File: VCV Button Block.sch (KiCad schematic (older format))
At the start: 20 parts, among them SW41 B3F-5050, SW42 B3F-5050, SW43 B3F-5050, SW44 B3F-5050, SW45 B3F-5050, SW46 B3F-5050, SW47 B3F-5050, SW48 B3F-5050, SW49 B3F-5050, SW50 B3F-5050, SW51 B3F-5050, SW52 B3F-5050, SW53 B3F-5050, SW54 B3F-5050, SW55 B3F-5050, SW56 B3F-5050, U4 CD74HC4067M

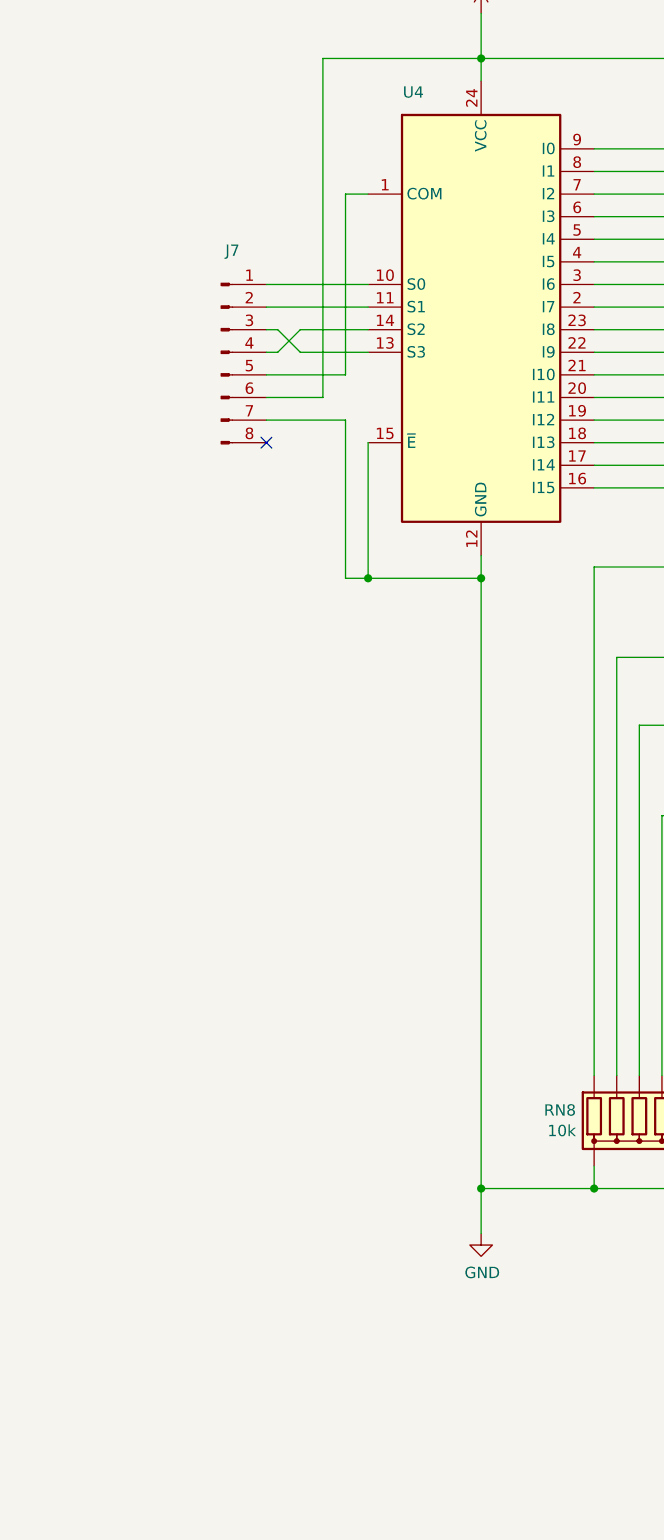
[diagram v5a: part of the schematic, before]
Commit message: Further cleanup and placement
Removed all the connectors to the rails as they're irrelevant to the top boards.

Added all the support headers.

Need to work out the correct routing for the headers but the placement is correct.
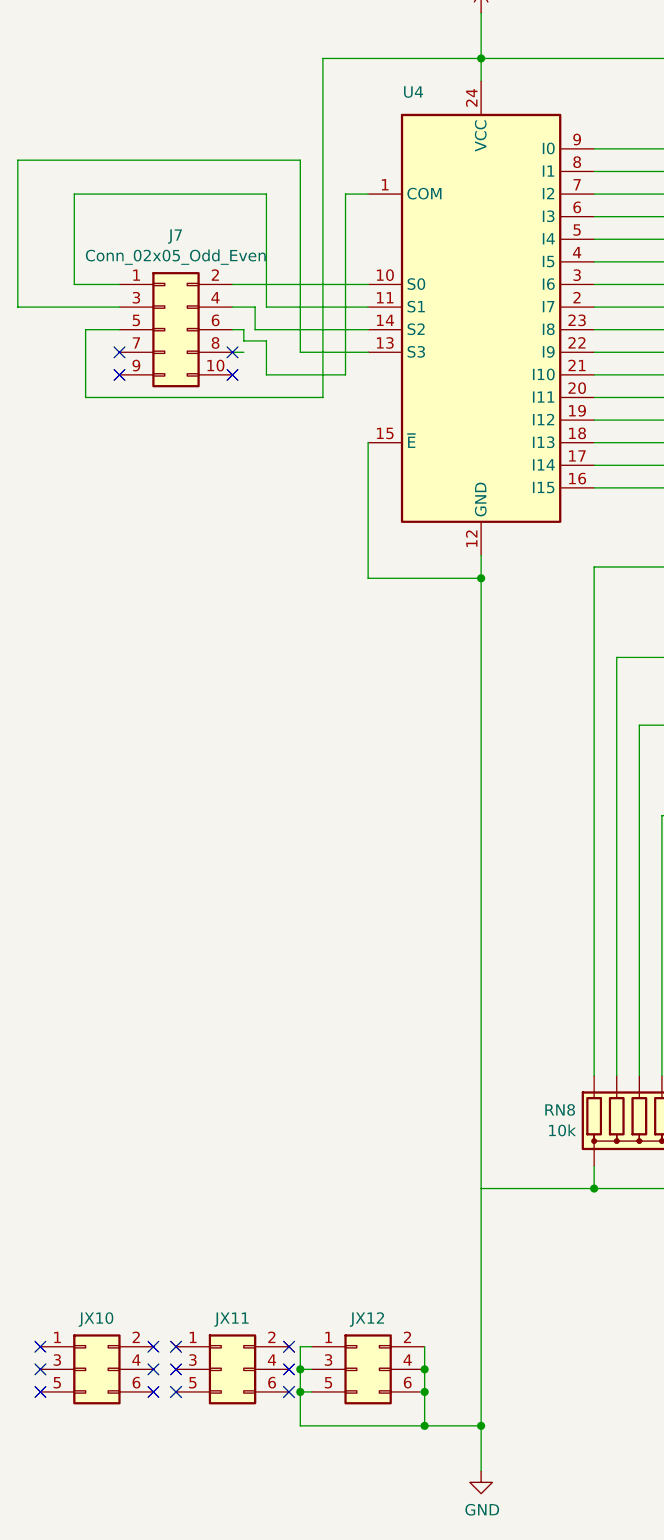
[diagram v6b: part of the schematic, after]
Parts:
- removed J7: ~, cunabulapress-footprints:Connector_TE_Connectivity_Micro-MaTch_8_Position_Female, symbol Connector:Conn_01x08_Male
- added J7: Conn_02x05_Odd_Even, Connector_PinHeader_2.54mm:PinHeader_2x05_P2.54mm_Vertical, symbol Connector_Generic:Conn_02x05_Odd_Even
- added JX10, JX11, JX12: Conn_02x03_Odd_Even, Connector_PinHeader_2.54mm:PinHeader_2x03_P2.54mm_Vertical, symbol Connector_Generic:Conn_02x03_Odd_Even
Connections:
- net +5V: now also J7.5 (Pin_5)
- net GND: now also JX12.1 (Pin_1), JX12.2 (Pin_2), JX12.3 (Pin_3), JX12.4 (Pin_4), JX12.5 (Pin_5), JX12.6 (Pin_6); no longer RN8.1 (common), RN9.1 (common)
- net at U4.1 (COM): now also J7.6 (Pin_6)
- net at U4.10 (S0): now also J7.2 (Pin_2)
- net at U4.11 (S1): now also J7.1 (Pin_1)
- net at U4.13 (S3): now also J7.3 (Pin_3)
- net at U4.14 (S2): now also J7.4 (Pin_4)
- new net: RN8.1 (common), RN9.1 (common)
- no-connect marks 33 -> 48
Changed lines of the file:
@@
 $Descr A4 11693 8268
 encoding utf-8
-Sheet 9 9
+Sheet 8 8
 Title ""
 Date ""
-Rev ""
+Rev "v3"
 Comp ""
 Comment1 ""
@@
 	1    0    0    -1
 $EndComp
-$Comp
-L power:GND #PWR?
-U 1 1 5C60FBB6
-P 2700 6350
-AR Path="/5C4B73B3/5C60FBB6" Ref="#PWR?"  Part="1"
-AR Path="/5C4BAA18/5C60FBB6" Ref="#PWR022"  Part="1"
-F 0 "#PWR022" H 2700 6100 50  0001 C CNN
-F 1 "GND" H 2705 6177 50  0000 C CNN
-F 2 "" H 2700 6350 50  0001 C CNN
-F 3 "" H 2700 6350 50  0001 C CNN
-	1    2700 6350
-	1    0    0    -1
-$EndComp
 Wire Wire Line
 	2200 2850 2200 3450
@@
 	2700 950  2700 1150
 NoConn ~ 7700 2500
-$Comp
-L Connector:Conn_01x08_Male J?
-U 1 1 5CE6340D
-P 1550 2450
-AR Path="/5C3B66BD/5CE6340D" Ref="J?"  Part="1"
-AR Path="/5C4BAA18/5CE6340D" Ref="J7"  Part="1"
-F 0 "J7" H 1600 2900 50  0000 C CNN
-F 1 "~" H 1444 2844 50  0000 C CNN
-F 2 "cunabulapress-footprints:Connector_TE_Connectivity_Micro-MaTch_8_Position_Female" H 1550 2450 50  0001 C CNN
-F 3 "~" H 1550 2450 50  0001 C CNN
-	1    1550 2450
-	1    0    0    -1
-$EndComp
-NoConn ~ 1750 2850
 Wire Wire Line
 	2000 2650 2000 1150
@@
 Wire Wire Line
 	2700 1150 2700 1250
-Wire Wire Line
-	1750 2350 1800 2350
-Wire Wire Line
-	1800 2350 1900 2450
-Wire Wire Line
-	1900 2350 1800 2450
-Wire Wire Line
-	1800 2450 1750 2450
 Connection ~ 2700 3450
 NoConn ~ 7300 2500
@@
 $EndComp
 Wire Wire Line
-	1750 2650 2000 2650
-Wire Wire Line
-	2700 3450 2700 6150
-Wire Wire Line
 	3200 3050 4000 3050
 Wire Wire Line
@@
 	3200 6150 2700 6150
 Wire Wire Line
-	2700 6150 2700 6350
-Connection ~ 2700 6150
-Wire Wire Line
 	7100 2600 7300 2600
 Wire Wire Line
@@
 	7700 5400 7900 5400
 Wire Wire Line
-	2200 3450 2100 3450
-Wire Wire Line
-	2100 3450 2100 2750
-Connection ~ 2200 3450
+	2100 2550 2100 1750
+Wire Wire Line
+	2100 1750 2200 1750
+Wire Wire Line
+	2000 1150 2700 1150
 Wire Wire Line
 	1750 2550 2100 2550
 Wire Wire Line
-	2100 2550 2100 1750
-Wire Wire Line
-	2100 1750 2200 1750
-Wire Wire Line
 	1900 2450 2200 2450
 Wire Wire Line
-	1900 2350 2200 2350
-Wire Wire Line
 	1750 2250 2200 2250
-Wire Wire Line
-	1750 2150 2200 2150
-Wire Wire Line
-	1750 2750 2100 2750
-Wire Wire Line
-	2000 1150 2700 1150
+$Comp
+L Connector_Generic:Conn_02x05_Odd_Even J?
+U 1 1 5D6E6331
+P 1300 2350
+AR Path="/5C4B73B3/5D6E6331" Ref="J?"  Part="1"
+AR Path="/5C4BAA18/5D6E6331" Ref="J7"  Part="1"
+F 0 "J7" H 1350 2767 50  0000 C CNN
+F 1 "Conn_02x05_Odd_Even" H 1350 2676 50  0000 C CNN
+F 2 "Connector_PinHeader_2.54mm:PinHeader_2x05_P2.54mm_Vertical" H 1300 2350 50  0001 C CNN
+F 3 "~" H 1300 2350 50  0001 C CNN
+	1    1300 2350
+	1    0    0    -1
+$EndComp
+Wire Wire Line
+	1600 2150 2200 2150
+Wire Wire Line
+	1750 2250 1750 1750
+Wire Wire Line
+	1750 1750 900  1750
+Wire Wire Line
+	900  1750 900  2150
+Wire Wire Line
+	900  2150 1100 2150
+Wire Wire Line
+	1700 2350 1700 2250
+Wire Wire Line
+	1700 2250 1600 2250
+Wire Wire Line
+	1700 2350 2200 2350
+Wire Wire Line
+	1900 2450 1900 1600
+Wire Wire Line
+	1900 1600 650  1600
+Wire Wire Line
+	650  2250 1100 2250
+Wire Wire Line
+	1750 2550 1750 2400
+Wire Wire Line
+	1750 2400 1650 2400
+Wire Wire Line
+	1650 2400 1650 2350
+Wire Wire Line
+	1650 2350 1600 2350
+Wire Wire Line
+	950  2650 950  2350
+Wire Wire Line
+	950  2350 1100 2350
+Wire Wire Line
+	950  2650 2000 2650
+Wire Wire Line
+	1650 2450 1600 2450
+NoConn ~ 1100 2450
+NoConn ~ 1100 2550
+NoConn ~ 1600 2550
+NoConn ~ 1600 2450
+Wire Wire Line
+	650  1600 650  2250
+$Comp
+L power:GND #PWR?
+U 1 1 5D912B99
+P 2700 7400
+AR Path="/5C4B73B3/5D912B99" Ref="#PWR?"  Part="1"
+AR Path="/5C4BAA18/5D912B99" Ref="#PWR0103"  Part="1"
+F 0 "#PWR0103" H 2700 7150 50  0001 C CNN
+F 1 "GND" H 2705 7227 50  0000 C CNN
+F 2 "" H 2700 7400 50  0001 C CNN
+F 3 "" H 2700 7400 50  0001 C CNN
+	1    2700 7400
+	1    0    0    -1
+$EndComp
+$Comp
+L Connector_Generic:Conn_02x03_Odd_Even JX?
+U 1 1 5D912B9F
+P 950 6950
+AR Path="/5C4B73B3/5D912B9F" Ref="JX?"  Part="1"
+AR Path="/5C4BAA18/5D912B9F" Ref="JX10"  Part="1"
+F 0 "JX10" H 1000 7175 50  0000 C CNN
+F 1 "Conn_02x03_Odd_Even" H 1000 7176 50  0001 C CNN
+F 2 "Connector_PinHeader_2.54mm:PinHeader_2x03_P2.54mm_Vertical" H 950 6950 50  0001 C CNN
+F 3 "~" H 950 6950 50  0001 C CNN
+	1    950  6950
+	1    0    0    -1
+$EndComp
+$Comp
+L Connector_Generic:Conn_02x03_Odd_Even JX?
+U 1 1 5D912BA6
+P 2150 6950
+AR Path="/5C4B73B3/5D912BA6" Ref="JX?"  Part="1"
+AR Path="/5C4BAA18/5D912BA6" Ref="JX12"  Part="1"
+F 0 "JX12" H 2200 7175 50  0000 C CNN
+F 1 "Conn_02x03_Odd_Even" H 2200 7176 50  0001 C CNN
+F 2 "Connector_PinHeader_2.54mm:PinHeader_2x03_P2.54mm_Vertical" H 2150 6950 50  0001 C CNN
+F 3 "~" H 2150 6950 50  0001 C CNN
+	1    2150 6950
+	1    0    0    -1
+$EndComp
+Wire Wire Line
+	2700 7200 2700 7400
+Connection ~ 2700 7200
+Wire Wire Line
+	2450 6850 2450 6950
+Wire Wire Line
+	2450 7200 2700 7200
+Connection ~ 2450 6950
+Wire Wire Line
+	2450 6950 2450 7050
+Connection ~ 2450 7050
+Wire Wire Line
+	2450 7050 2450 7200
+$Comp
+L Connector_Generic:Conn_02x03_Odd_Even JX?
+U 1 1 5D912BB6
+P 1550 6950
+AR Path="/5C4B73B3/5D912BB6" Ref="JX?"  Part="1"
+AR Path="/5C4BAA18/5D912BB6" Ref="JX11"  Part="1"
+F 0 "JX11" H 1600 7175 50  0000 C CNN
+F 1 "Conn_02x03_Odd_Even" H 1600 7176 50  0001 C CNN
+F 2 "Connector_PinHeader_2.54mm:PinHeader_2x03_P2.54mm_Vertical" H 1550 6950 50  0001 C CNN
+F 3 "~" H 1550 6950 50  0001 C CNN
+	1    1550 6950
+	1    0    0    -1
+$EndComp
+Wire Wire Line
+	1900 6850 1900 6950
+Wire Wire Line
+	1900 7200 2450 7200
+Connection ~ 2450 7200
+Wire Wire Line
+	1950 7050 1900 7050
+Connection ~ 1900 7050
+Wire Wire Line
+	1900 7050 1900 7200
+Wire Wire Line
+	1950 6950 1900 6950
+Connection ~ 1900 6950
+Wire Wire Line
+	1900 6950 1900 7050
+Wire Wire Line
+	1950 6850 1900 6850
+NoConn ~ 1850 6850
+NoConn ~ 1850 6950
+NoConn ~ 1850 7050
+NoConn ~ 1350 7050
+NoConn ~ 1350 6950
+NoConn ~ 1350 6850
+NoConn ~ 1250 6850
+NoConn ~ 1250 6950
+NoConn ~ 1250 7050
+NoConn ~ 750  6850
+NoConn ~ 750  6950
+NoConn ~ 750  7050
+Wire Wire Line
+	2700 3450 2700 7200
 $EndSCHEMATC

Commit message: All subsidiary boards complete
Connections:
- net GND: now also RN8.1 (common), RN9.1 (common)
- net at U4.10 (S0): now also J7.1 (Pin_1); no longer J7.2 (Pin_2)
- net at U4.11 (S1): now also J7.2 (Pin_2); no longer J7.1 (Pin_1)
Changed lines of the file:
@@
 	3200 6050 3200 6150
-Wire Wire Line
-	3200 6150 2700 6150
 Wire Wire Line
 	7100 2600 7300 2600
@@
 Wire Wire Line
 	5600 6150 3200 6150
-Connection ~ 3200 6150
 Wire Wire Line
 	6400 2250 3200 2250
@@
 Wire Wire Line
 	1900 2450 2200 2450
-Wire Wire Line
-	1750 2250 2200 2250
 $Comp
 L Connector_Generic:Conn_02x05_Odd_Even J?
@@
 AR Path="/5C4BAA18/5D6E6331" Ref="J7"  Part="1"
 F 0 "J7" H 1350 2767 50  0000 C CNN
-F 1 "Conn_02x05_Odd_Even" H 1350 2676 50  0000 C CNN
+F 1 "Conn_02x05_Odd_Even" H 1350 2676 50  0001 C CNN
 F 2 "Connector_PinHeader_2.54mm:PinHeader_2x05_P2.54mm_Vertical" H 1300 2350 50  0001 C CNN
 F 3 "~" H 1300 2350 50  0001 C CNN
@@
 $EndComp
 Wire Wire Line
-	1600 2150 2200 2150
-Wire Wire Line
-	1750 2250 1750 1750
-Wire Wire Line
-	1750 1750 900  1750
-Wire Wire Line
-	900  1750 900  2150
-Wire Wire Line
-	900  2150 1100 2150
-Wire Wire Line
-	1700 2350 1700 2250
-Wire Wire Line
-	1700 2250 1600 2250
-Wire Wire Line
-	1700 2350 2200 2350
-Wire Wire Line
-	1900 2450 1900 1600
-Wire Wire Line
-	1900 1600 650  1600
-Wire Wire Line
-	650  2250 1100 2250
-Wire Wire Line
 	1750 2550 1750 2400
 Wire Wire Line
@@
 Wire Wire Line
 	950  2650 2000 2650
-Wire Wire Line
-	1650 2450 1600 2450
 NoConn ~ 1100 2450
 NoConn ~ 1100 2550
 NoConn ~ 1600 2550
 NoConn ~ 1600 2450
-Wire Wire Line
-	650  1600 650  2250
 $Comp
 L power:GND #PWR?
@@
 NoConn ~ 750  7050
 Wire Wire Line
-	2700 3450 2700 7200
+	2700 3450 2700 6150
+Wire Wire Line
+	2200 2150 2200 1900
+Wire Wire Line
+	2200 1900 900  1900
+Wire Wire Line
+	900  1900 900  2150
+Wire Wire Line
+	900  2150 1100 2150
+Wire Wire Line
+	1600 2150 2150 2150
+Wire Wire Line
+	2150 2150 2150 2250
+Wire Wire Line
+	2150 2250 2200 2250
+Wire Wire Line
+	2200 2350 1950 2350
+Wire Wire Line
+	1950 2350 1950 2250
+Wire Wire Line
+	1950 2250 1600 2250
+Wire Wire Line
+	1100 2250 1000 2250
+Wire Wire Line
+	1000 2250 1000 2000
+Wire Wire Line
+	1000 2000 1900 2000
+Wire Wire Line
+	1900 2000 1900 2450
+Wire Wire Line
+	3200 6150 2700 6150
+Connection ~ 3200 6150
+Connection ~ 2700 6150
+Wire Wire Line
+	2700 6150 2700 7200
 $EndSCHEMATC

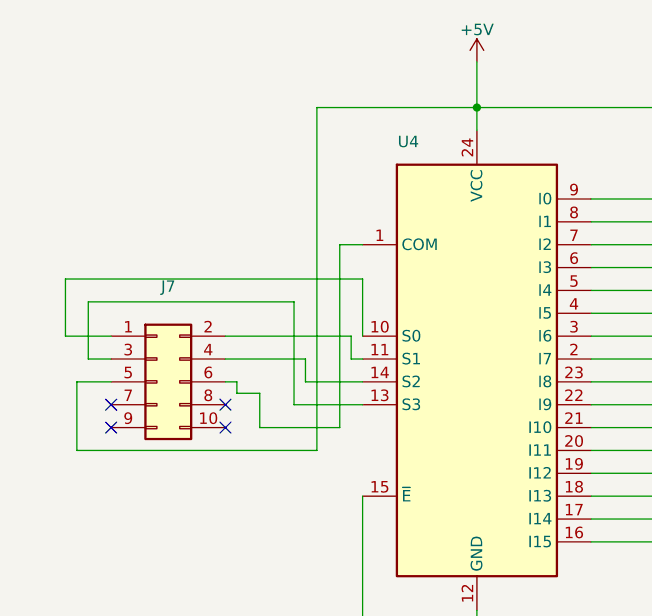
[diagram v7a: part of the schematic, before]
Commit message: Housekeeping
Cleaned up the schematic for the subsidiary boards

Switched 5v and Com connections to make routing easier.
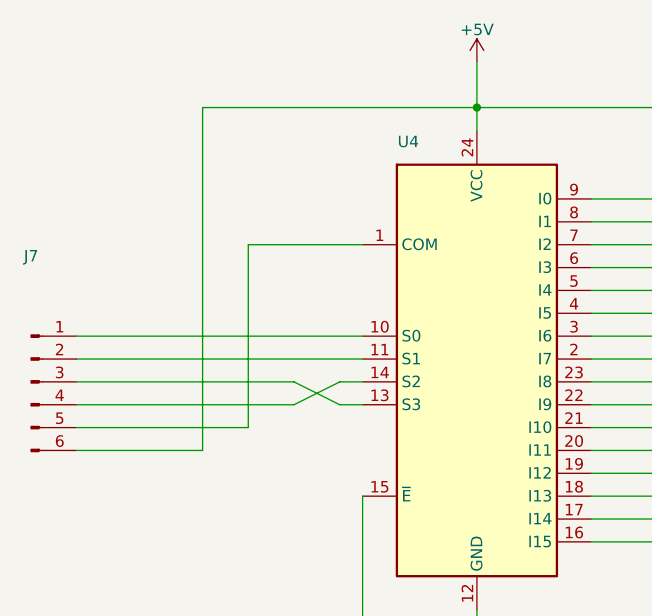
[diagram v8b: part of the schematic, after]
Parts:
- removed J7: Conn_02x05_Odd_Even, Connector_PinHeader_2.54mm:PinHeader_2x05_P2.54mm_Vertical, symbol Connector_Generic:Conn_02x05_Odd_Even
- added J7: Conn_02x05_Odd_Even, Connector_PinHeader_2.54mm:PinHeader_2x03_P2.54mm_Vertical, symbol Connector:Conn_01x06_Male
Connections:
- net +5V: now also J7.6 (Pin_6)
- net at U4.1 (COM): now also J7.5 (Pin_5)
- net at U4.10 (S0): now also J7.1 (Pin_1)
- net at U4.11 (S1): now also J7.2 (Pin_2)
- net at U4.13 (S3): now also J7.3 (Pin_3)
- net at U4.14 (S2): now also J7.4 (Pin_4)
- no-connect marks 48 -> 44
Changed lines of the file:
@@
-	1    0    0    -1
-$EndComp
-$Comp
-L 74xx:CD74HC4067M U?
-U 1 1 5C60FB42
-P 2700 2250
-AR Path="/5C4B73B3/5C60FB42" Ref="U?"  Part="1"
-AR Path="/5C4BAA18/5C60FB42" Ref="U4"  Part="1"
-F 0 "U4" H 2400 3200 50  0000 C CNN
-F 1 "CD74HC4067M" H 2700 3337 50  0001 C CNN
-F 2 "Package_SO:SOIC-24W_7.5x15.4mm_P1.27mm" H 3600 1250 50  0001 C CIN
-F 3 "http://www.ti.com/lit/ds/symlink/cd74hc4067.pdf" H 2350 3100 50  0001 C CNN
-	1    2700 2250
 	1    0    0    -1
 $EndComp
@@
 	2700 950  2700 1150
 NoConn ~ 7700 2500
-Wire Wire Line
-	2000 2650 2000 1150
 Connection ~ 2700 1150
 Wire Wire Line
@@
 Wire Wire Line
 	7700 5400 7900 5400
-Wire Wire Line
-	2100 2550 2100 1750
-Wire Wire Line
-	2100 1750 2200 1750
-Wire Wire Line
-	2000 1150 2700 1150
-Wire Wire Line
-	1750 2550 2100 2550
-Wire Wire Line
-	1900 2450 2200 2450
-$Comp
-L Connector_Generic:Conn_02x05_Odd_Even J?
-U 1 1 5D6E6331
-P 1300 2350
-AR Path="/5C4B73B3/5D6E6331" Ref="J?"  Part="1"
-AR Path="/5C4BAA18/5D6E6331" Ref="J7"  Part="1"
-F 0 "J7" H 1350 2767 50  0000 C CNN
-F 1 "Conn_02x05_Odd_Even" H 1350 2676 50  0001 C CNN
-F 2 "Connector_PinHeader_2.54mm:PinHeader_2x05_P2.54mm_Vertical" H 1300 2350 50  0001 C CNN
-F 3 "~" H 1300 2350 50  0001 C CNN
-	1    1300 2350
-	1    0    0    -1
-$EndComp
-Wire Wire Line
-	1750 2550 1750 2400
-Wire Wire Line
-	1750 2400 1650 2400
-Wire Wire Line
-	1650 2400 1650 2350
-Wire Wire Line
-	1650 2350 1600 2350
-Wire Wire Line
-	950  2650 950  2350
-Wire Wire Line
-	950  2350 1100 2350
-Wire Wire Line
-	950  2650 2000 2650
-NoConn ~ 1100 2450
-NoConn ~ 1100 2550
-NoConn ~ 1600 2550
-NoConn ~ 1600 2450
 $Comp
 L power:GND #PWR?
@@
 	2700 3450 2700 6150
 Wire Wire Line
-	2200 2150 2200 1900
-Wire Wire Line
-	2200 1900 900  1900
-Wire Wire Line
-	900  1900 900  2150
-Wire Wire Line
-	900  2150 1100 2150
-Wire Wire Line
-	1600 2150 2150 2150
-Wire Wire Line
-	2150 2150 2150 2250
-Wire Wire Line
-	2150 2250 2200 2250
-Wire Wire Line
-	2200 2350 1950 2350
-Wire Wire Line
-	1950 2350 1950 2250
-Wire Wire Line
-	1950 2250 1600 2250
-Wire Wire Line
-	1100 2250 1000 2250
-Wire Wire Line
-	1000 2250 1000 2000
-Wire Wire Line
-	1000 2000 1900 2000
-Wire Wire Line
-	1900 2000 1900 2450
-Wire Wire Line
 	3200 6150 2700 6150
 Connection ~ 3200 6150
@@
 Wire Wire Line
 	2700 6150 2700 7200
+$Comp
+L 74xx:CD74HC4067M U?
+U 1 1 5C60FB42
+P 2700 2250
+AR Path="/5C4B73B3/5C60FB42" Ref="U?"  Part="1"
+AR Path="/5C4BAA18/5C60FB42" Ref="U4"  Part="1"
+F 0 "U4" H 2400 3200 50  0000 C CNN
+F 1 "CD74HC4067M" H 2700 3337 50  0001 C CNN
+F 2 "Package_SO:SOIC-24W_7.5x15.4mm_P1.27mm" H 3600 1250 50  0001 C CIN
+F 3 "http://www.ti.com/lit/ds/symlink/cd74hc4067.pdf" H 2350 3100 50  0001 C CNN
+	1    2700 2250
+	1    0    0    -1
+$EndComp
+$Comp
+L Connector:Conn_01x06_Male J?
+U 1 1 5D7A7D01
+P 750 2350
+AR Path="/5C4B73B3/5D7A7D01" Ref="J?"  Part="1"
+AR Path="/5C4BAA18/5D7A7D01" Ref="J7"  Part="1"
+F 0 "J7" H 750 2900 50  0000 C CNN
+F 1 "Conn_02x05_Odd_Even" H 800 2676 50  0001 C CNN
+F 2 "Connector_PinHeader_2.54mm:PinHeader_2x03_P2.54mm_Vertical" H 750 2350 50  0001 C CNN
+F 3 "~" H 750 2350 50  0001 C CNN
+	1    750  2350
+	1    0    0    -1
+$EndComp
+Wire Wire Line
+	2200 2150 950  2150
+Wire Wire Line
+	950  2250 2200 2250
+Wire Wire Line
+	950  2550 1700 2550
+Wire Wire Line
+	1700 2550 1700 1750
+Wire Wire Line
+	1700 1750 2200 1750
+Wire Wire Line
+	950  2650 1500 2650
+Wire Wire Line
+	1500 2650 1500 1150
+Wire Wire Line
+	1500 1150 2700 1150
+Wire Wire Line
+	1900 2450 950  2450
+Wire Wire Line
+	950  2350 1900 2350
+Wire Wire Line
+	2100 2350 2200 2350
+Wire Wire Line
+	2100 2450 2200 2450
+Wire Wire Line
+	1900 2350 2100 2450
+Wire Wire Line
+	2100 2350 1900 2450
 $EndSCHEMATC
